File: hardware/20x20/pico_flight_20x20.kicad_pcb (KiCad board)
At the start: 2 copper layers, 28 x 28 mm, 49 parts, among them J1 USB_B_Micro, J2 Conn_01x02, J3 DEBUG, J4 ESC_AIKON32, J5 UART1, J6 UART2, J7 CAM, J8 VTX, U1 MCP1711T-33I_OT, U2 W25Q128JVS, U3 RP2040, U4 MPU-9250, Y1 SMD-3225_4P__12MHZ_20PF_10PPM

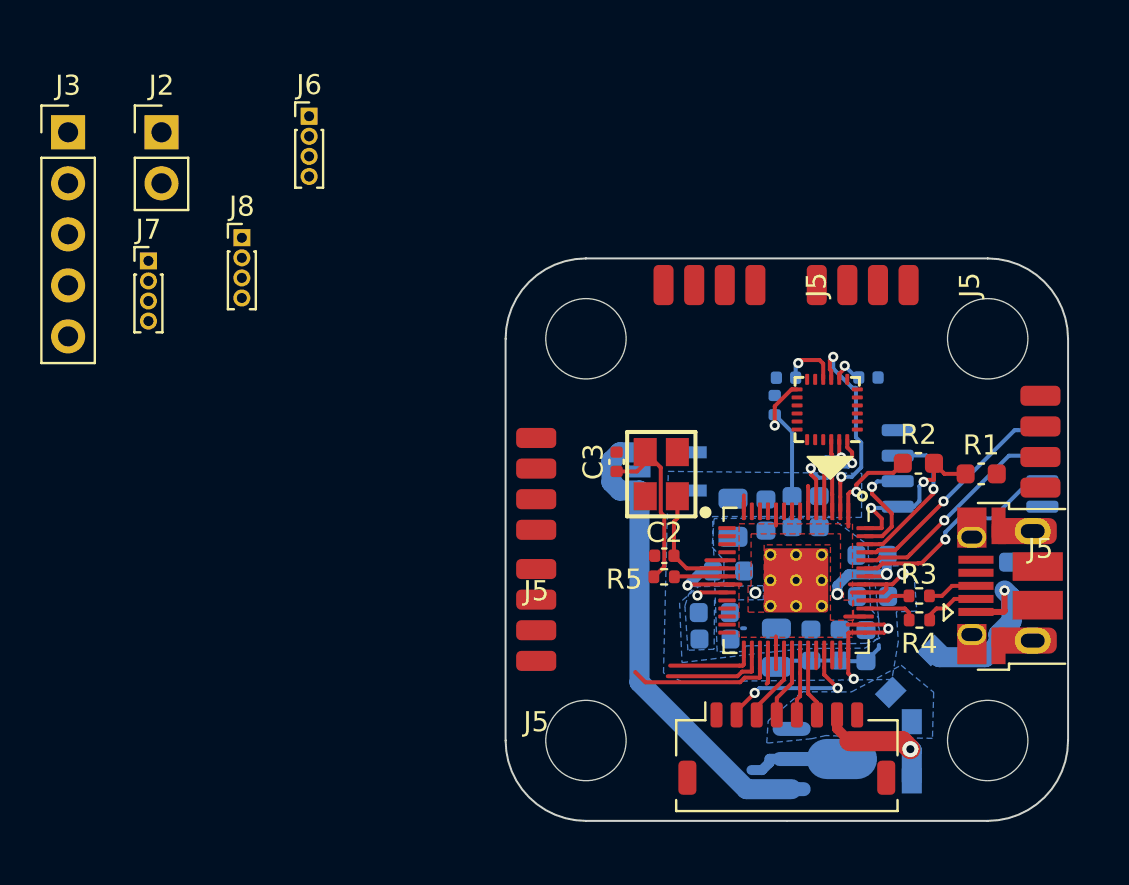
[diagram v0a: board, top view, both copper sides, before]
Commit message: Update to kicad 6 more progress on 20x20 board layout
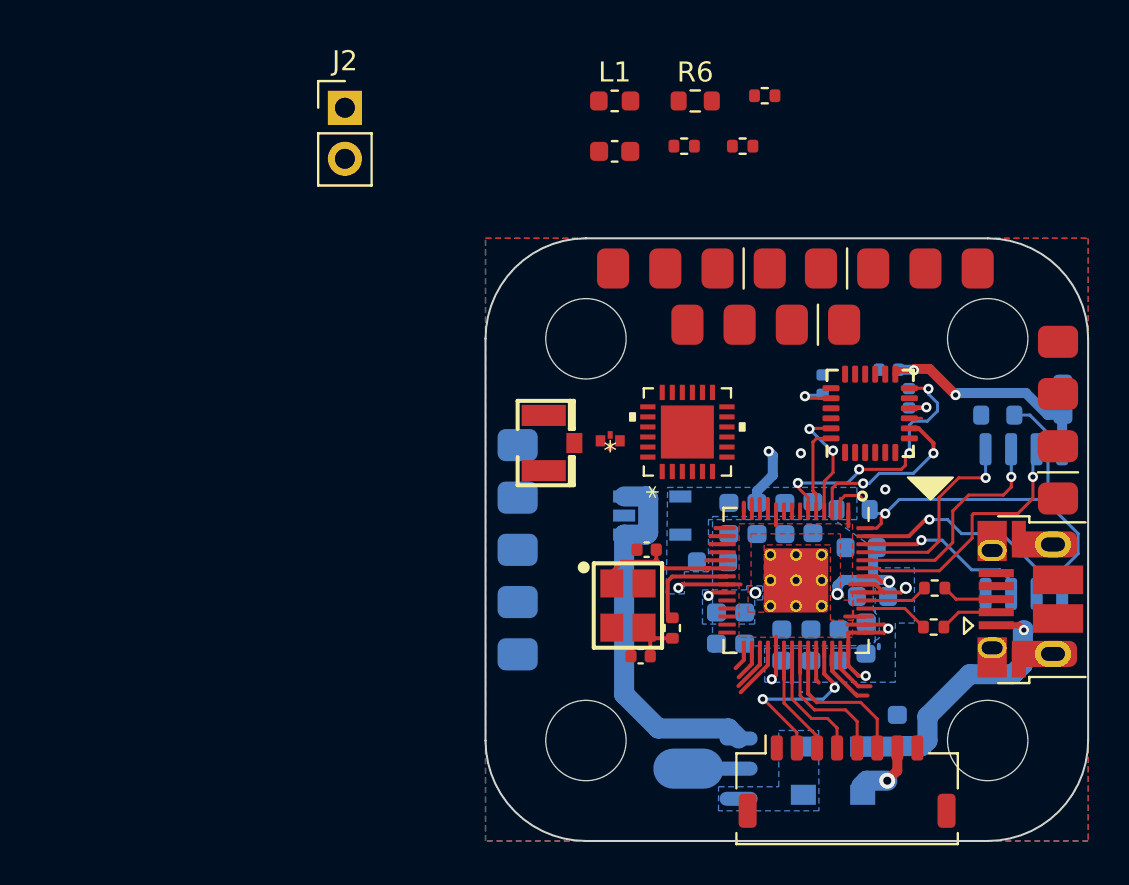
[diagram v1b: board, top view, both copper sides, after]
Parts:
- removed the J5 at (22.6, 9.95)
- removed the J5 at (18.6, -2.67)
- removed the J5 at (11.0, -2.67)
- removed the J5 at (-2.48, 12.1)
- removed the J5 at (-2.48, 18.6)
- added C21: 100n, Capacitor_SMD:C_0402_1005Metric, B.Cu at (15.1, 1.54)
- added C22: 2.2nf, Capacitor_SMD:C_0402_1005Metric, B.Cu at (11.8, 2.28)
- added C23: 100n, Capacitor_SMD:C_0402_1005Metric, B.Cu at (16.1, 2.96)
- added C24: 10nF, Capacitor_SMD:C_0603_1608Metric, F.Cu at (1.43, -9.33)
- added J5: UART1, pico-flight:PAD_X4_SMD_03x02, F.Cu at (12.8, -0.70)
- added L1: 15uH, Inductor_SMD:L_0603_1608Metric, F.Cu at (1.43, -11.8)
- added R6: 0, Resistor_SMD:R_0603_1608Metric, F.Cu at (5.44, -11.8)
- added U5: MPU-6000, Sensor_Motion:InvenSense_QFN-24_4x4mm_P0.5mm, F.Cu at (14.2, 3.71)
- added U6: 2450FM07A0035T_JOT, 01-pico-footprints:2450FM07A0035T, F.Cu at (1.21, 5.08)
- added X1: ANTENNA_U.FL, 01-pico-footprints:U.FL, F.Cu at (-2.10, 5.19)
- C17, C4: footprint Capacitor_SMD:C_0805_2012Metric -> Capacitor_SMD:C_0603_1608Metric
- C18: value 10nF -> 470nF; footprint Capacitor_SMD:C_0402_1005Metric -> Resistor_SMD:R_0402_1005Metric; moved to F.Cu
- C19: value 0.1uF -> 10nF; footprint Capacitor_SMD:C_0402_1005Metric -> Resistor_SMD:R_0402_1005Metric; moved to F.Cu
- C20: value 0.1uF -> 470nF; footprint Capacitor_SMD:C_0402_1005Metric -> Resistor_SMD:R_0402_1005Metric; moved to F.Cu
- J3: footprint Connector_PinHeader_2.54mm:PinHeader_1x05_P2.54mm_Vertical -> pico-flight:PAD_X5_SMD_03x02; moved to B.Cu
- J6: footprint Connector_PinHeader_1.00mm:PinHeader_1x04_P1.00mm_Vertical -> pico-flight:PAD_X4_SMD_03x02
- J7: value CAM -> UART3; footprint Connector_PinHeader_1.00mm:PinHeader_1x04_P1.00mm_Vertical -> pico-flight:PAD_X4_SMD_03x02
- J8: value VTX -> UART4; footprint Connector_PinHeader_1.00mm:PinHeader_1x04_P1.00mm_Vertical -> pico-flight:PAD_X4_SMD_03x02
- R1: footprint Capacitor_SMD:C_0603_1608Metric -> Resistor_SMD:R_0603_1608Metric; moved to B.Cu
- R2: value DNF -> 1k; footprint Capacitor_SMD:C_0603_1608Metric -> Resistor_SMD:R_0603_1608Metric; moved to B.Cu
- U3: footprint pico-flight:RP2040-QFN-56 -> 01-pico-footprints:RP2040-QFN-56
- U4: value MPU-9250 -> QFN24_4X4_SEM; footprint Sensor_Motion:InvenSense_QFN-24_3x3mm_P0.4mm -> 01-pico-footprints:SX1280IMLTRT
- moved J7 46.8 mm to (23.5, 7.95)
- moved J3 34.3 mm to (-3.40, 15.7), turned to 180 degrees
- moved J8 28.9 mm to (11.7, -3.50), turned to -90 degrees
- moved J6 24.2 mm to (9.15, -3.50), turned to 90 degrees
- moved C18 14.9 mm to (8.90, -12.1), turned to 0 degrees
- moved C19 13.0 mm to (7.80, -9.59), turned to 0 degrees
- moved C20 12.6 mm to (4.89, -9.59), turned to 0 degrees
- moved C3 9.75 mm to (2.72, 15.8), turned to 180 degrees
- moved J2 9.21 mm to (-12.0, -11.5)
- moved C1 8.85 mm to (15.5, 19.5), turned to 90 degrees
- moved C5 8.34 mm to (23.7, 3.01), turned to 90 degrees
- moved U4 7.05 mm to (5.05, 4.64), turned to 90 degrees
- moved Y1 6.75 mm to (2.09, 13.3), turned to -90 degrees
- moved D2 5.41 mm to (12.3, 20.3), turned to 0 degrees
- moved D1 4.48 mm to (12.3, 22.7), turned to 0 degrees
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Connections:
- net /~USB_BOOT renamed /~{USB_BOOT}
- net Net-(J7-Pad2) renamed UART3_TX
- net Net-(J7-Pad4) renamed UART3_RX
- net Net-(J8-Pad2) renamed UART4_TX
- net Net-(J8-Pad4) renamed UART4_RX
- net Net-(U3-Pad38) renamed ADC0
- net Net-(U3-Pad40) renamed ADC2
- net Net-(U3-Pad41) renamed ADC3
- C18 pad 1: GND -> Net-(U4-Pad12)
- C18 pad 2: +3V3 -> GND
- C19 pad 1: GND -> Net-(U4-Pad12)
- C19 pad 2: +3V3 -> GND
- C20 pad 1: Net-(C20-Pad1) -> Net-(U4-Pad11)
- J1 pad 4: Net-(J1-Pad4) -> unconnected-(J1-Pad4)
- J6 pad 2: UART2_RX -> UART2_TX
- J6 pad 4: UART2_TX -> UART2_RX
- U1 pad 4: Net-(U1-Pad4) -> unconnected-(U1-Pad4)
- U3 pad 11: Net-(U3-Pad11) -> unconnected-(U3-Pad11)
- U3 pad 12: Net-(U3-Pad12) -> unconnected-(U3-Pad12)
- U3 pad 13: Net-(U3-Pad13) -> unconnected-(U3-Pad13)
- U3 pad 14: Net-(U3-Pad14) -> unconnected-(U3-Pad14)
- U3 pad 15: Net-(U3-Pad15) -> unconnected-(U3-Pad15)
- U3 pad 16: Net-(U3-Pad16) -> unconnected-(U3-Pad16)
- U3 pad 17: Net-(U3-Pad17) -> unconnected-(U3-Pad17)
- U3 pad 18: Net-(U3-Pad18) -> unconnected-(U3-Pad18)
- U3 pad 27: Net-(U3-Pad27) -> unconnected-(U3-Pad27)
- U3 pad 28: Net-(U3-Pad28) -> unconnected-(U3-Pad28)
- U3 pad 29: Net-(U3-Pad29) -> unconnected-(U3-Pad29)
- U3 pad 30: Net-(U3-Pad30) -> unconnected-(U3-Pad30)
- U3 pad 7: Net-(U3-Pad7) -> unconnected-(U3-Pad7)
- U3 pad 8: Net-(U3-Pad8) -> unconnected-(U3-Pad8)
- U3 pad 9: Net-(U3-Pad9) -> unconnected-(U3-Pad9)
- U4 pad 1: +3V3 -> Net-(U4-Pad1)
- U4 pad 10: Net-(C20-Pad1) -> unconnected-(U4-Pad10)
- U4 pad 12: IMU_DATA_RDY -> Net-(U4-Pad12)
- U4 pad 13: +3V3 -> GND
- U4 pad 14: (no net) -> Net-(U4-Pad14)
- U4 pad 15: (no net) -> +3V3
- U4 pad 16: (no net) -> unconnected-(U4-Pad16)
- U4 pad 17: (no net) -> unconnected-(U4-Pad17)
- U4 pad 18: GND -> unconnected-(U4-Pad18)
- U4 pad 19: (no net) -> unconnected-(U4-Pad19)
- U4 pad 2: (no net) -> Net-(U4-Pad12)
- U4 pad 21: Net-(U4-Pad21) -> GND
- U4 pad 22: IMU_SPI_CS -> Net-(U4-Pad22)
- U4 pad 23: IMU_SPI_SCLK -> GND
- U4 pad 24: IMU_SPI_MOSI -> GND
- U4 pad 3: (no net) -> unconnected-(U4-Pad3)
- U4 pad 4: (no net) -> unconnected-(U4-Pad4)
- U4 pad 5: (no net) -> GND
- U4 pad 6: (no net) -> unconnected-(U4-Pad6)
- U4 pad 7: Net-(U4-Pad7) -> unconnected-(U4-Pad7)
- U4 pad 8: +3V3 -> unconnected-(U4-Pad8)
- U4 pad 9: IMU_SPI_MISO -> unconnected-(U4-Pad9)
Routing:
- net /QSPI_SS: track 8.82 -> 22.6 mm, vias 2 -> 1
- net IMU_DATA_RDY: track 2.10 -> 13.9 mm, vias 0 -> 4
- net IMU_SPI_MISO: track 10.3 -> 3.27 mm, vias 2 -> 0
- net /QSPI_SD1: track 5.30 -> 11.2 mm
- net Net-(C3-Pad1): track 8.97 -> 3.18 mm
- net UART1_RX: track 7.91 -> 2.27 mm
- net Net-(U3-Pad30): track 5.38 -> 0.00 mm
- net IMU_SPI_CS: track 3.59 -> 8.92 mm, vias 0 -> 2
- net +5V: track 23.5 -> 18.7 mm
- net Net-(U3-Pad29): track 4.44 -> 0.00 mm
- net ESC_MOTOR_1: track 3.44 -> 7.60 mm
- net +3V3: track 38.4 -> 34.2 mm, vias 7 -> 8
- net Net-(C1-Pad1): track 9.71 -> 13.5 mm
- net ESC_MOTOR_2: track 3.33 -> 6.99 mm
- net VBAT: track 6.37 -> 3.25 mm
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- added copper zone on F.Cu, net GND
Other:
- board size 28 x 28 mm -> 30 x 30 mm
- net class Default removed

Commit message: latest kicad files
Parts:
- added C25: 10u, Capacitor_SMD:C_0603_1608Metric, B.Cu at (16.3, -0.30)
- added U7: MCP1711T-33I_OT, Package_TO_SOT_SMD:SOT-23-5, B.Cu at (11.5, -1.20)
- C18, C19, C20, C24, L1: moved to B.Cu
- C5: footprint Capacitor_SMD:C_0603_1608Metric -> Capacitor_SMD:C_0402_1005Metric
- J2: footprint Connector_PinHeader_2.54mm:PinHeader_1x02_P2.54mm_Vertical -> 01-pico-footprints:PAD_X2_SMD_01x02; moved to B.Cu
- J5, J6, J7, J8: footprint pico-flight:PAD_X4_SMD_03x02 -> 01-pico-footprints:PAD_X4_SMD_03x02
- R1, R2: footprint Resistor_SMD:R_0603_1608Metric -> Resistor_SMD:R_0402_1005Metric
- R6: footprint Resistor_SMD:R_0603_1608Metric -> Resistor_SMD:R_0402_1005Metric; moved to B.Cu
- U1: footprint lc_lib:SOT-23-5 -> Package_TO_SOT_SMD:SOT-23-5
- U4: value QFN24_4X4_SEM -> SX1280IMLTRT
- U6: value 2450FM07A0035T_JOT -> 2450FM07A0035T
- moved J2 45.6 mm to (23.5, 17.1)
- moved R6 17.4 mm to (9.20, 5.10), turned to 90 degrees
- moved C18 15.3 mm to (7.40, 3.10), turned to 90 degrees
- moved C19 14.6 mm to (7.40, 5.00), turned to -90 degrees
- moved C24 14.5 mm to (1.20, 5.20), turned to -90 degrees
- moved L1 13.9 mm to (7.40, 0.70), turned to -90 degrees
- moved C20 13.5 mm to (9.20, 3.20), turned to 90 degrees
- moved R1 10.7 mm to (23.5, 14.1), turned to 0 degrees
- moved J7 6.93 mm to (23.5, 1.02), turned to 180 degrees
- moved U1 6.23 mm to (3.51, 15.0), turned to 90 degrees
- moved R2 6.15 mm to (16.6, 13.7)
- moved J4 3.99 mm to (9.05, 21.4)
- moved C3 1.94 mm to (1.81, 14.1)
- moved Y1 1.94 mm to (1.18, 11.6)
- moved R5 1.93 mm to (3.55, 12.6)
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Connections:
- C21 pad 1: +3V3 -> +3.3VADC
- U3 pad 11: unconnected-(U3-Pad11) -> /RF_DIO_3
- U3 pad 12: unconnected-(U3-Pad12) -> /RF_DIO_2
- U3 pad 13: unconnected-(U3-Pad13) -> /RF_DIO_1
- U3 pad 14: unconnected-(U3-Pad14) -> /RF_BUSY
- U3 pad 15: unconnected-(U3-Pad15) -> /RF_SPI_MISO
- U3 pad 16: unconnected-(U3-Pad16) -> /RF_SPI_CS
- U3 pad 17: unconnected-(U3-Pad17) -> /RF_SPI_SCLK
- U3 pad 18: unconnected-(U3-Pad18) -> /RF_SPI_MOSI
- U3 pad 31: UART1_RX -> unconnected-(U3-Pad31)
- U3 pad 32: UART1_TX -> unconnected-(U3-Pad32)
- U3 pad 6: IMU_DATA_RDY -> UART1_TX
- U3 pad 7: unconnected-(U3-Pad7) -> UART1_RX
- U3 pad 8: unconnected-(U3-Pad8) -> IMU_DATA_RDY
- U3 pad 9: unconnected-(U3-Pad9) -> /RF_NRESET
- U4 pad 10: unconnected-(U4-Pad10) -> /RF_DIO_3
- U4 pad 16: unconnected-(U4-Pad16) -> /RF_SPI_MISO
- U4 pad 17: unconnected-(U4-Pad17) -> /RF_SPI_MOSI
- U4 pad 18: unconnected-(U4-Pad18) -> /RF_SPI_SCLK
- U4 pad 19: unconnected-(U4-Pad19) -> /RF_SPI_CS
- U4 pad 3: unconnected-(U4-Pad3) -> /RF_NRESET
- U4 pad 7: unconnected-(U4-Pad7) -> /RF_BUSY
- U4 pad 8: unconnected-(U4-Pad8) -> /RF_DIO_1
- U4 pad 9: unconnected-(U4-Pad9) -> /RF_DIO_2
- U5 pad 13: +3V3 -> +3.3VADC
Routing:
- net +5V: track 18.7 -> 81.6 mm, vias 0 -> 4
- net Net-(C18-Pad1): track 0.00 -> 23.1 mm, vias 0 -> 4
- net SWCLK: track 0.00 -> 14.7 mm, vias 0 -> 1
- net /RF_SPI_MOSI: track 0.00 -> 13.9 mm, vias 0 -> 2
- net /RF_SPI_SCLK: track 0.00 -> 12.6 mm, vias 0 -> 2
- net /RF_SPI_CS: track 0.00 -> 12.1 mm, vias 0 -> 2
- net SWDIO: track 0.00 -> 11.4 mm, vias 0 -> 1
- net /RF_SPI_MISO: track 0.00 -> 11.3 mm, vias 0 -> 2
- net +3V3: track 34.2 -> 24.6 mm, vias 8 -> 4
- net UART1_RX: track 2.27 -> 11.5 mm
- net UART1_TX: track 2.70 -> 10.8 mm
- net +3.3VADC: track 0.00 -> 7.21 mm, vias 0 -> 1
- net IMU_SPI_MISO: track 3.27 -> 9.95 mm, vias 0 -> 2
- net /RF_DIO_3: track 0.00 -> 6.27 mm
- net /~{USB_BOOT}: track 0.00 -> 5.90 mm
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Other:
- board text added: "5V"
- board text added: "G"
